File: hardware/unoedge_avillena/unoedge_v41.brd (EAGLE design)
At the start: 73.7 x 44.6 mm, 6 parts, among them X1 53047-06

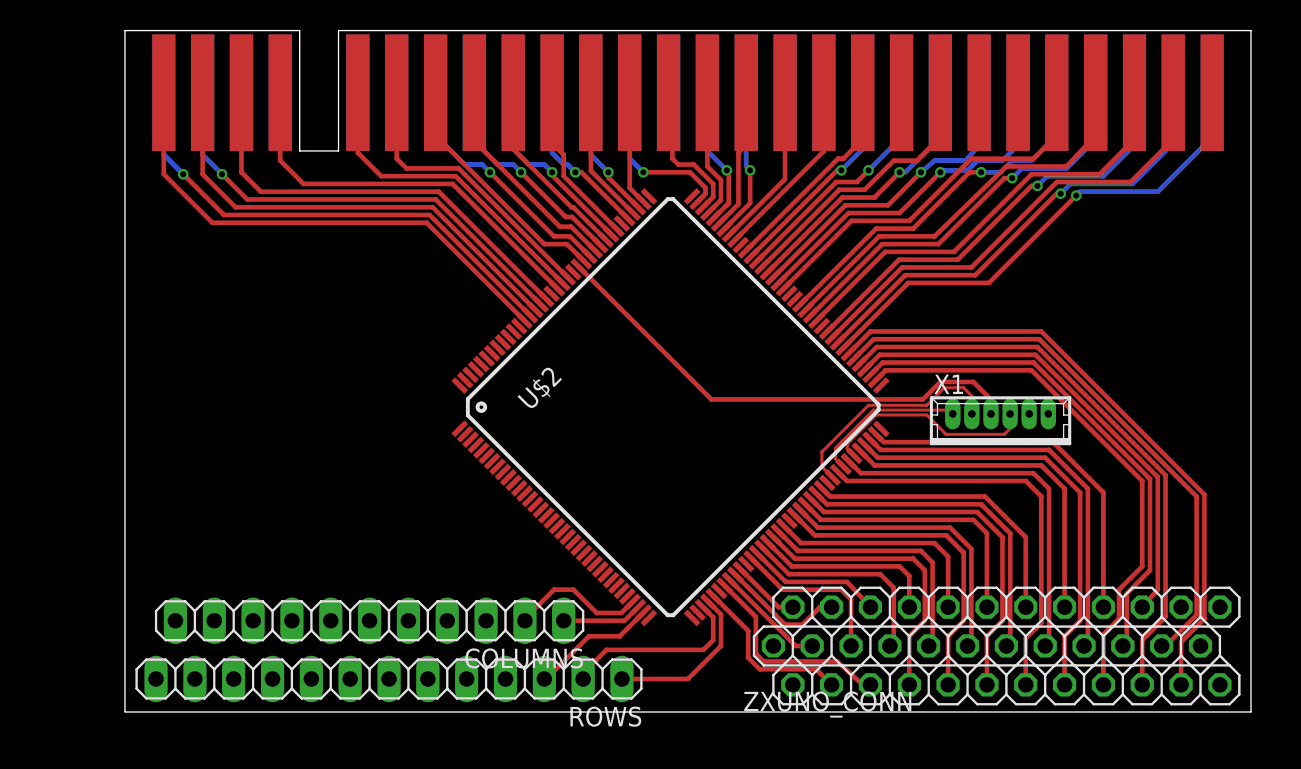
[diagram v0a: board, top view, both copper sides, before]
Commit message: Roto chip para añadir GCLK
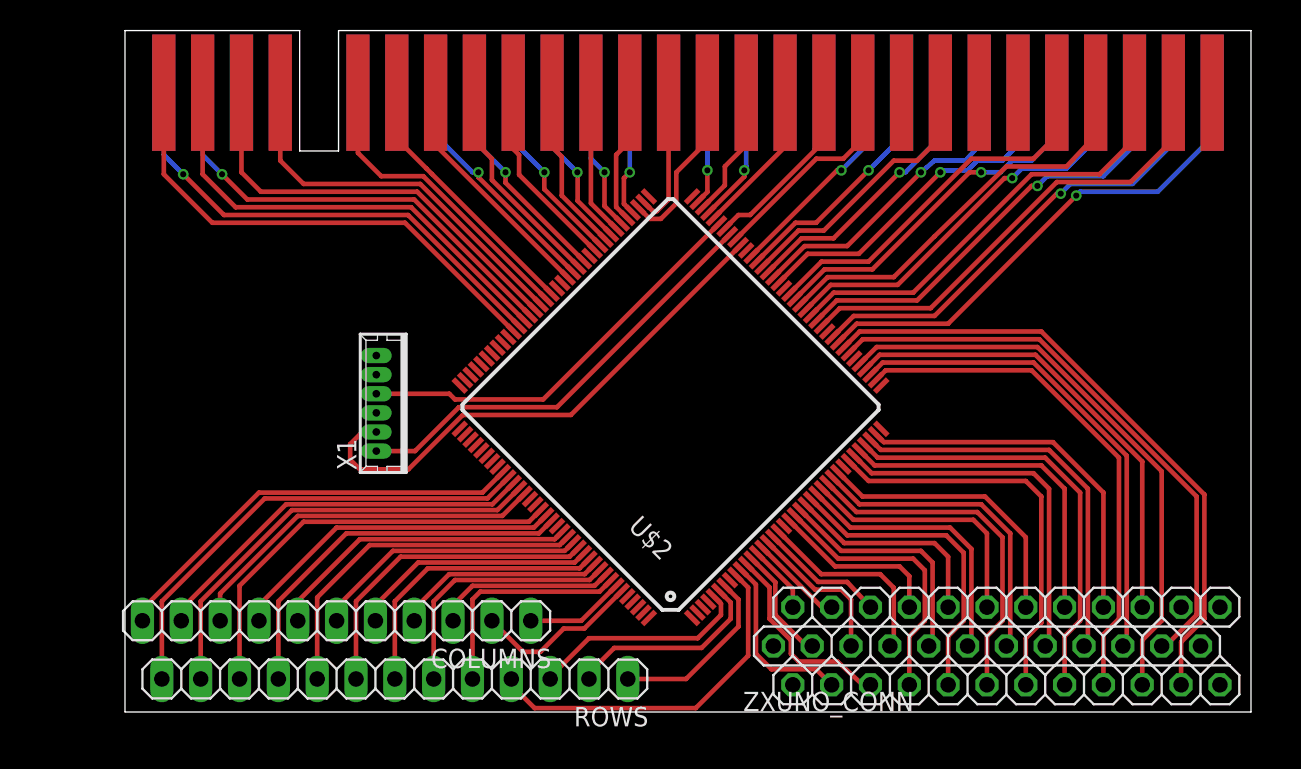
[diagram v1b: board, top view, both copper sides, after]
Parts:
- moved X1 40.4 mm to (16.9, 20.2), turned to 90 degrees
- moved COLUMNS 2.16 mm to (13.8, 5.97)
- moved ROWS 0.38 mm to (17.7, 2.16)
- turned U$2 to 135 degrees
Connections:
- net /BUSACK: now also U$2.49; no longer U$2.83
- net /BUSRQ: now also U$2.61; no longer U$2.97
- net /HALT: now also U$2.75
- net /INT: now also U$2.77
- net /IORQ: now also U$2.68
- net /M1: now also U$2.54; no longer U$2.91
- net /MREQ: now also U$2.70
- net /NMI: now also U$2.74
- net /RD: now also U$2.66
- net /RESET: now also U$2.60; no longer U$2.96
- net /RFSH: now also U$2.52; no longer U$2.87
- net /WAIT: now also U$2.59; no longer U$2.95
- net /WR: now also U$2.64; no longer U$2.98
- net /Y: now also U$2.69
- net A0: now also U$2.85; no longer U$2.118
- net A1: now also U$2.82
- net A10: now also U$2.48; no longer U$2.82
- net A11: now also U$2.45; no longer U$2.80
- net A12: now also U$2.95; no longer U$2.129
- net A13: now also U$2.96; no longer U$2.130
- net A14: now also U$2.97; no longer U$2.131
- net A15: now also U$2.98; no longer U$2.132
- net A2: now also U$2.80
- net A3: now also U$2.78
- net A4: now also U$2.53; no longer U$2.88
- net A5: now also U$2.56; no longer U$2.92
- net A6: now also U$2.57; no longer U$2.93
- net A7: now also U$2.58; no longer U$2.94
- net A8: now also U$2.50; no longer U$2.85
- net A9: now also U$2.46; no longer U$2.81
- net C1: now also U$2.138; no longer U$2.34
- net C10: now also U$2.119
- net C11: now also U$2.117
- net C2: now also U$2.139; no longer U$2.33
- net C3: now also U$2.136
- net C4: now also U$2.134
- net C5: now also U$2.132
- net C6: now also U$2.130
- net C7: now also U$2.128
- net C8: now also U$2.125
- net C9: now also U$2.121
- net D0: now also U$2.92; no longer U$2.125
- net D1: now also U$2.91; no longer U$2.124
- net D2: now also U$2.88; no longer U$2.121
- net D3: now also U$2.81
- net D4: now also U$2.79
- net D5: now also U$2.83; no longer U$2.117
- net D6: now also U$2.86; no longer U$2.119
- net D7: now also U$2.94; no longer U$2.128
- net IORQGE: now also U$2.76
- net P10: now also U$2.11; no longer U$2.43
- net P11: now also U$2.15; no longer U$2.48
- net P12: now also U$2.16; no longer U$2.49
- net P13: now also U$2.20; no longer U$2.52
- net P14: now also U$2.17; no longer U$2.50
- net P15: now also U$2.19; no longer U$2.51
- net P16: now also U$2.23; no longer U$2.56
- net P17: now also U$2.21; no longer U$2.53
- net P18: now also U$2.22; no longer U$2.54
- net P19: now also U$2.26; no longer U$2.59
- net P20: now also U$2.24; no longer U$2.57
- net P21: now also U$2.25; no longer U$2.58
- net P22: now also U$2.30; no longer U$2.64
- net P23: now also U$2.27; no longer U$2.60
- net P24: now also U$2.28; no longer U$2.61
- net P25: now also U$2.33; no longer U$2.69
- net P26: now also U$2.31; no longer U$2.66
- net P27: now also U$2.32; no longer U$2.68
- net P28: now also U$2.38; no longer U$2.74
- net P29: now also U$2.34; no longer U$2.70
- net P30: now also U$2.35; no longer U$2.71
- net P31: now also U$2.41; no longer U$2.77
- net P32: now also U$2.39; no longer U$2.75
- net P33: now also U$2.40; no longer U$2.76
- net P34: now also U$2.44; no longer U$2.79
- net P35: now also U$2.43; no longer U$2.78
- net P6: now also U$2.13; no longer U$2.46
- net P7: now also U$2.10; no longer U$2.41
- net P8: now also U$2.12; no longer U$2.44
- net P9: now also U$2.14; no longer U$2.45
- net R1: now also U$2.7; no longer U$2.40
- net R10: now also U$2.126
- net R11: now also U$2.124
- net R12: now also U$2.120
- net R13: now also U$2.118
- net R2: now also U$2.6; no longer U$2.39
- net R3: now also U$2.5; no longer U$2.35
- net R4: now also U$2.9
- net R5: now also U$2.137
- net R6: now also U$2.135
- net R7: now also U$2.133
- net R8: now also U$2.131
- net R9: now also U$2.129
- net ROM1OE: now also U$2.93; no longer U$2.126
- net ROM2OE: now also U$2.71
- net ROMCS: now also U$2.51; no longer U$2.86
- net SPCLK: now also U$2.87; no longer U$2.120
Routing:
- net TDO: track 32.6 -> 0.00 mm
- net R13: track 0.00 -> 31.1 mm
- net R12: track 0.00 -> 29.0 mm
- net C11: track 0.00 -> 28.1 mm
- net R11: track 0.00 -> 27.9 mm
- net C10: track 0.00 -> 25.9 mm
- net R10: track 0.00 -> 25.1 mm
- net C9: track 0.00 -> 24.4 mm
- net R4: track 0.00 -> 23.6 mm
- net R9: track 0.00 -> 23.4 mm
- net C8: track 0.00 -> 22.2 mm
- net R8: track 0.00 -> 21.1 mm
- net C7: track 0.00 -> 20.5 mm
- net TDI: track 14.9 -> 34.9 mm
- net R7: track 0.00 -> 19.0 mm
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
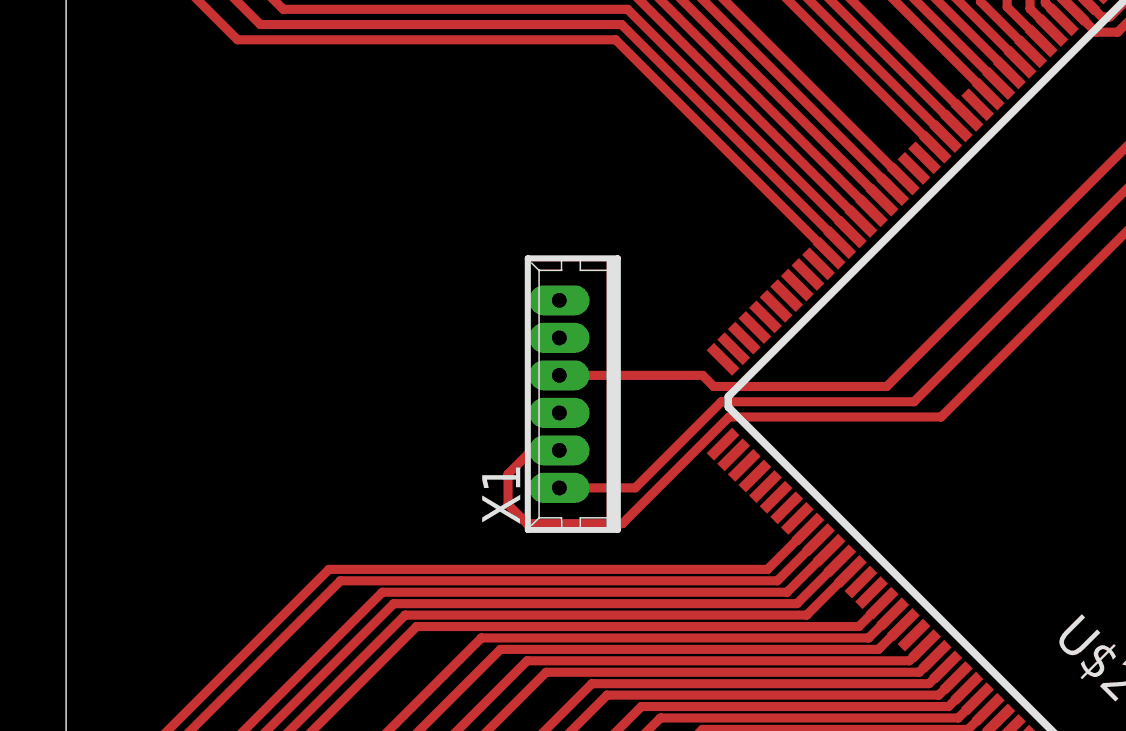
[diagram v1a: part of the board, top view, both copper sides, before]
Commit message: Me faltan condensadores de desacoplo y alimentación de 12V
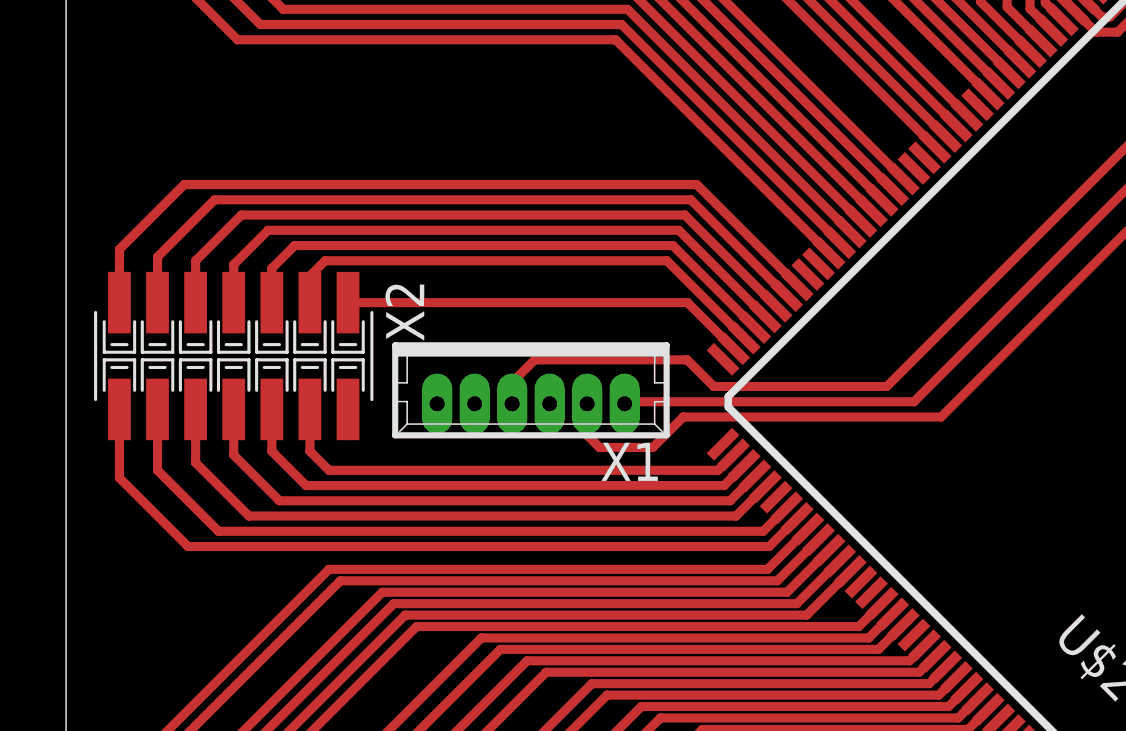
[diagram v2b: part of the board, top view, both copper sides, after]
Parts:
- added X2: 1296-T14, con-leotronics:1296-14
- moved X1 1.40 mm to (15.5, 20.3), turned to 180 degrees
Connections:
- new net E1: U$2.116, X2.14
- new net E10: U$2.104, X2.7
- new net E11: U$2.103, X2.9
- new net E12: U$2.102, X2.11
- new net E13: U$2.101, X2.13
- new net E2: U$2.115, X2.12
- new net E3: U$2.113, X2.10
- new net E4: U$2.112, X2.8
- new net E5: U$2.111, X2.6
- new net E6: U$2.110, X2.4
- new net E7: U$2.107, X2.1
- new net E8: U$2.106, X2.3
- new net E9: U$2.105, X2.5
- net /HALT: no longer U$2.105
- net /INT: no longer U$2.110
- net /IORQ: no longer U$2.101
- net /MREQ: no longer U$2.103
- net /NMI: no longer U$2.106
- net /RD: no longer U$2.100
- net /Y: no longer U$2.102
- net A1: no longer U$2.116
- net A2: no longer U$2.113
- net A3: no longer U$2.111
- net D3: no longer U$2.115
- net D4: no longer U$2.112
- net GND: now also X2.2
- net IORQGE: no longer U$2.107
- net ROM2OE: no longer U$2.104
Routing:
- net E13: track 0.00 -> 26.7 mm
- net E1: track 0.00 -> 26.2 mm
- net E12: track 0.00 -> 24.6 mm
- net E2: track 0.00 -> 24.2 mm
- net E11: track 0.00 -> 22.6 mm
- net E3: track 0.00 -> 21.9 mm
- net E10: track 0.00 -> 20.7 mm
- net E4: track 0.00 -> 19.9 mm
- net E9: track 0.00 -> 18.7 mm
- net E5: track 0.00 -> 17.9 mm
- net E8: track 0.00 -> 16.6 mm
- net E6: track 0.00 -> 16.0 mm
- net E7: track 0.00 -> 13.5 mm
- net TDI: track 34.9 -> 29.2 mm
- net TMS: track 29.0 -> 25.7 mm
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
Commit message: Creo que ya está
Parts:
- added C1, C2: (no value), rcl:C0805
- added C3, C4, C5, C6: 100nf, rcl:C0603
- added IC1: REG1117, burr-brown:SOT223
- added JP1: (no value), pinhead:1X04
- moved X1 0.25 mm to (15.5, 20.6)
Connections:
- new net 3.3V: ZXUNO_CONN.3.3V@1, ZXUNO_CONN.3.3V@2
- net +12V: now also JP1.4
- net +3.3V: now also C2.1, IC1.2; no longer ZXUNO_CONN.3.3V@1, ZXUNO_CONN.3.3V@2
- net +3V3: now also C3.1, C4.1, C5.1, C6.1
- net +5V: now also C1.1, IC1.3, JP1.1
- net GND: now also C1.2, C2.2, C3.2, C4.2, C5.2, C6.2, IC1.1, JP1.2, JP1.3
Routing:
- net GND: track 0.00 -> 199.1 mm, vias 0 -> 12
- net +5V: track 0.00 -> 119.2 mm, vias 0 -> 1
- net +3V3: track 0.00 -> 101.0 mm, vias 0 -> 7
- net +12V: track 0.00 -> 68.6 mm, vias 0 -> 1
- net TDO: track 0.00 -> 15.7 mm, vias 0 -> 1
- net +3.3V: track 0.00 -> 3.90 mm
- added copper zone on layer 16, net GND

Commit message: Continuación unoedge
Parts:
- removed X2: 1296-T14, con-leotronics:1296-14
- added R1, R2, R3, R4, R5, R6: (no value), rcl:R0603
- added RN1: (no value), resistor-sil:SIL9
- added SD1: TF-HOLDER, sd-mmc:TF-PULL
- moved X1 4.26 mm to (17.4, 24.4), turned to 90 degrees
- moved COLUMNS 1.02 mm to (13.7, 6.99)
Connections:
- removed net E1: U$2.116, X2.14
- removed net E2: U$2.115, X2.12
- removed net E3: U$2.113, X2.10
- new net N$2: R6.1, SD1.8
- new net N$3: R5.1, SD1.1
- new net SD_CLK: SD1.5
- new net SD_CS: SD1.2
- new net SD_MISO: R4.1, SD1.7
- new net SD_MOSI: SD1.3
- net +3V3: now also R1.1, R2.1, R3.1, R4.2, R5.2, R6.2, RN1.1, SD1.4
- net C1: now also RN1.9, U$2.136; no longer U$2.138
- net C10: now also R2.2, U$2.116; no longer U$2.119
- net C11: now also R3.2, U$2.113; no longer U$2.117
- net C2: now also RN1.8, U$2.135; no longer U$2.139
- net C3: now also RN1.7, U$2.133; no longer U$2.136
- net C4: now also RN1.6, U$2.131; no longer U$2.134
- net C5: now also RN1.5, U$2.129; no longer U$2.132
- net C6: now also RN1.4, U$2.126; no longer U$2.130
- net C7: now also RN1.3, U$2.124; no longer U$2.128
- net C8: now also RN1.2, U$2.120; no longer U$2.125
- net C9: now also R1.2, U$2.118; no longer U$2.121
- net E10: no longer X2.7
- net E11: no longer X2.9
- net E12: no longer X2.11
- net E13: no longer X2.13
- net E4: no longer X2.8
- net E5: no longer X2.6
- net E6: no longer X2.4
- net E7: no longer X2.1
- net E8: no longer X2.3
- net E9: no longer X2.5
- net GND: now also SD1.6, SD1.S1, SD1.S2, SD1.S3, SD1.S4; no longer X2.2
- net R10: now also U$2.121; no longer U$2.126
- net R11: now also U$2.119; no longer U$2.124
- net R12: now also U$2.117; no longer U$2.120
- net R13: now also U$2.115; no longer U$2.118
- net R5: now also U$2.134; no longer U$2.137
- net R6: now also U$2.132; no longer U$2.135
- net R7: now also U$2.130; no longer U$2.133
- net R8: now also U$2.128; no longer U$2.131
- net R9: now also U$2.125; no longer U$2.129
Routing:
- net E13: track 26.7 -> 0.00 mm
- net E1: track 26.2 -> 0.00 mm
- net E12: track 24.6 -> 0.00 mm
- net E2: track 24.2 -> 0.00 mm
- net E11: track 22.6 -> 0.00 mm
- net E3: track 21.9 -> 0.00 mm
- net E10: track 20.7 -> 0.00 mm
- net E4: track 19.9 -> 0.00 mm
- net E9: track 18.7 -> 0.00 mm
- net E5: track 17.9 -> 0.00 mm
- net E8: track 16.6 -> 0.00 mm
- net E6: track 16.0 -> 0.00 mm
- net E7: track 13.5 -> 0.00 mm
- net +3V3: track 101.0 -> 106.9 mm
- net TDI: track 28.9 -> 33.4 mm
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
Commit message: Acabado unoedge
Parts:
- added RN2: 10K, resistor-sil:SIL9
- R1, R2, R3, R4, R5, R6, RN1: value (none) -> 10K
- moved R5 14.3 mm to (8.76, 22.7), turned to 180 degrees
- moved R6 14.0 mm to (8.76, 18.2), turned to 180 degrees
- moved R4 13.6 mm to (8.76, 20.4), turned to 180 degrees
- moved JP1 0.76 mm to (5.59, 29.7)
- moved X1 0.13 mm to (17.4, 24.3)
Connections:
- removed net E4: U$2.112
- removed net E5: U$2.111
- removed net E6: U$2.110
- removed net E7: U$2.107
- net +5V: now also RN2.1
- net A12: now also U$2.96; no longer U$2.95
- net A13: now also U$2.95; no longer U$2.96
- net D0: now also RN2.3
- net D1: now also RN2.4
- net D2: now also RN2.5
- net D3: now also RN2.8
- net D4: now also RN2.9
- net D5: now also RN2.7
- net D6: now also RN2.6
- net D7: now also RN2.2
- net GND: no longer SD1.S2, SD1.S3
- net SD_CLK: now also U$2.111
- net SD_CS: now also U$2.107
- net SD_MISO: now also U$2.112
- net SD_MOSI: now also U$2.110
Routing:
- net +3V3: track 106.9 -> 154.5 mm, vias 7 -> 11
- net SD_MISO: track 0.00 -> 19.7 mm, vias 0 -> 2
- net GND: track 196.4 -> 208.4 mm
- net SD_CS: track 0.00 -> 10.2 mm, vias 0 -> 1
- net SD_CLK: track 0.00 -> 8.83 mm, vias 0 -> 1
- net SD_MOSI: track 0.00 -> 8.80 mm, vias 0 -> 1
- net N$2: track 0.00 -> 8.46 mm, vias 0 -> 1
- net N$3: track 0.00 -> 5.46 mm, vias 0 -> 1
- net D1: track 17.3 -> 20.9 mm
- net D2: track 15.7 -> 19.0 mm
- net D0: track 20.2 -> 23.2 mm
- net D6: track 14.2 -> 16.9 mm
- net D5: track 12.5 -> 15.0 mm
- net +12V: track 68.6 -> 70.8 mm
- net +5V: track 119.8 -> 121.9 mm
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
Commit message: Arreglo bug línea +3.3V aislada
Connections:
- removed net +3.3V: C2.1, IC1.2
- net +3V3: now also C2.1, IC1.2
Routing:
- net +3V3: track 154.5 -> 179.4 mm, vias 11 -> 13
- net +3.3V: track 3.90 -> 0.00 mm
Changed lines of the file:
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@@
 <wire x1="7.874" y1="16.383" x2="4.445" y2="16.383" width="0.4064" layer="1"/>
 <wire x1="4.445" y1="16.383" x2="4.318" y2="16.51" width="0.4064" layer="1"/>
+<contactref element="IC1" pad="2"/>
+<contactref element="C2" pad="1"/>
+<wire x1="69.4944" y1="22.9464" x2="68.58" y2="22.032" width="0.4064" layer="1"/>
+<wire x1="69.4944" y1="22.9464" x2="69.4944" y2="23.5966" width="0.4064" layer="1"/>
+<wire x1="69.4944" y1="23.5966" x2="69.469" y2="23.622" width="0.4064" layer="1"/>
+<via x="69.469" y="23.622" extent="1-16" drill="0.4"/>
+<wire x1="69.469" y1="23.622" x2="60.96" y2="23.622" width="0.4064" layer="16"/>
+<wire x1="60.96" y1="23.622" x2="58.928" y2="21.59" width="0.4064" layer="16"/>
+<via x="58.928" y="21.59" extent="1-16" drill="0.4"/>
+<wire x1="58.928" y1="21.59" x2="49.71236875" y2="21.59" width="0.4064" layer="1"/>
+<wire x1="49.71236875" y1="21.59" x2="49.47558125" y2="21.3532125" width="0.4064" layer="1"/>
+<wire x1="69.4944" y1="25.5524" x2="69.4944" y2="23.6474" width="0.4064" layer="1"/>
+<wire x1="69.4944" y1="23.6474" x2="69.469" y2="23.622" width="0.4064" layer="1"/>
 </signal>
 <signal name="D4">
@@
 <wire x1="32.639" y1="33.239903125" x2="33.212053125" y2="32.66685" width="0.3048" layer="1"/>
 </signal>
-<signal name="+3.3V">
-<contactref element="IC1" pad="2"/>
-<contactref element="C2" pad="1"/>
-<wire x1="69.4944" y1="25.5524" x2="69.4944" y2="22.9464" width="0.4064" layer="1"/>
-<wire x1="69.4944" y1="22.9464" x2="68.58" y2="22.032" width="0.4064" layer="1"/>
-</signal>
 <signal name="/HALT" class="1">
